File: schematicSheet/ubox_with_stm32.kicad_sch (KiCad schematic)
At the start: 14 parts, among them U3 SAM-M10Q-00B

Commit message: Arranged pin
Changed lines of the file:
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@@
 		(effects
 			(font
-				(size 1.27 1.27)
+				(size 0.889 0.889)
 			)
 			(justify left)
@@
 		(effects
 			(font
-				(size 1.27 1.27)
+				(size 0.889 0.889)
 			)
 			(justify left)
@@
 			(effects
 				(font
-					(size 1.27 1.27)
+					(size 0.889 0.889)
 				)
 				(justify left)
@@
 			(effects
 				(font
-					(size 1.27 1.27)
+					(size 0.889 0.889)
 				)
 				(justify left)
@@
 			(effects
 				(font
-					(size 1.27 1.27)
+					(size 0.889 0.889)
 				)
 			)
@@
 			(effects
 				(font
-					(size 1.27 1.27)
+					(size 0.889 0.889)
 				)
 				(justify left)
@@
 			(effects
 				(font
-					(size 1.27 1.27)
+					(size 0.889 0.889)
 				)
 				(justify left)
@@
 			(effects
 				(font
-					(size 1.27 1.27)
+					(size 0.889 0.889)
 				)
 			)
@@
 			(effects
 				(font
-					(size 1.27 1.27)
+					(size 0.889 0.889)
 				)
 			)
@@
 			(effects
 				(font
-					(size 1.27 1.27)
+					(size 0.889 0.889)
 				)
 			)
@@
 			(effects
 				(font
-					(size 1.27 1.27)
+					(size 0.889 0.889)
 				)
 			)
@@
 			(effects
 				(font
-					(size 1.27 1.27)
+					(size 0.889 0.889)
 				)
 				(justify right)
@@
 			(effects
 				(font
-					(size 1.27 1.27)
+					(size 0.889 0.889)
 				)
 				(justify right)
@@
 			(effects
 				(font
-					(size 1.27 1.27)
+					(size 0.889 0.889)
 				)
 				(justify right)
@@
 			(effects
 				(font
-					(size 1.27 1.27)
+					(size 0.889 0.889)
 				)
 				(justify right)
@@
 			(effects
 				(font
-					(size 1.27 1.27)
+					(size 0.889 0.889)
 				)
 			)
@@
 			(effects
 				(font
-					(size 1.27 1.27)
+					(size 0.889 0.889)
 				)
 			)
@@
 			(effects
 				(font
-					(size 1.27 1.27)
+					(size 0.889 0.889)
 				)
 			)
@@
 			(effects
 				(font
-					(size 1.27 1.27)
+					(size 0.889 0.889)
 				)
 			)
@@
 			(effects
 				(font
-					(size 1.27 1.27)
+					(size 0.889 0.889)
 				)
 				(justify left)
@@
 			(effects
 				(font
-					(size 1.27 1.27)
+					(size 0.889 0.889)
 				)
 				(justify left)
@@
 			(effects
 				(font
-					(size 1.27 1.27)
+					(size 0.889 0.889)
 				)
 			)
@@
 			(effects
 				(font
-					(size 1.27 1.27)
+					(size 0.889 0.889)
 				)
 			)
@@
 			(effects
 				(font
-					(size 1.27 1.27)
+					(size 0.889 0.889)
 				)
 				(justify left)
@@
 			(effects
 				(font
-					(size 1.27 1.27)
+					(size 0.889 0.889)
 				)
 				(justify left)
@@
 			(effects
 				(font
-					(size 1.27 1.27)
+					(size 0.889 0.889)
 				)
 			)
@@
 			(effects
 				(font
-					(size 1.27 1.27)
+					(size 0.889 0.889)
 				)
 			)
@@
 			(effects
 				(font
-					(size 1.524 1.524)
+					(size 0.889 0.889)
 				)
 			)
@@
 			(effects
 				(font
-					(size 1.524 1.524)
+					(size 0.889 0.889)
 				)
 			)
@@
 			(effects
 				(font
-					(size 1.27 1.27)
+					(size 0.889 0.889)
 				)
 				(justify right)
@@
 			(effects
 				(font
-					(size 1.27 1.27)
+					(size 0.889 0.889)
 				)
 				(justify right)
@@
 			(effects
 				(font
-					(size 1.27 1.27)
+					(size 0.889 0.889)
 				)
 			)
@@
 			(effects
 				(font
-					(size 1.27 1.27)
+					(size 0.889 0.889)
 				)
 			)
@@
 			(effects
 				(font
-					(size 1.27 1.27)
+					(size 0.889 0.889)
 				)
 			)
@@
 			(effects
 				(font
-					(size 1.27 1.27)
+					(size 0.889 0.889)
 				)
 			)
@@
 			(effects
 				(font
-					(size 1.27 1.27)
+					(size 0.889 0.889)
 				)
 			)
@@
 			(effects
 				(font
-					(size 1.27 1.27)
+					(size 0.889 0.889)
 				)
 				(justify left)
@@
 			(effects
 				(font
-					(size 1.27 1.27)
+					(size 0.889 0.889)
 				)
 				(justify left)

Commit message: update
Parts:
- C1, C2: footprint Capacitor_SMD:C_0805_2012Metric -> Capacitor_SMD:C_0402_1005Metric
- R1, R2, R3, R8, R9: footprint Resistor_SMD:R_0805_2012Metric -> Resistor_SMD:R_0402_1005Metric
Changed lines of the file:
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@@
 			)
 		)
-		(property "Footprint" "Resistor_SMD:R_0805_2012Metric"
+		(property "Footprint" "Resistor_SMD:R_0402_1005Metric"
 			(at 117.602 124.46 90)
 			(effects
@@
 			)
 		)
-		(property "Footprint" "Capacitor_SMD:C_0805_2012Metric"
+		(property "Footprint" "Capacitor_SMD:C_0402_1005Metric"
 			(at 100.0252 60.96 0)
 			(effects
@@
 			)
 		)
-		(property "Footprint" "Resistor_SMD:R_0805_2012Metric"
+		(property "Footprint" "Resistor_SMD:R_0402_1005Metric"
 			(at 203.2 59.182 90)
 			(effects
@@
 			)
 		)
-		(property "Footprint" "Capacitor_SMD:C_0805_2012Metric"
+		(property "Footprint" "Capacitor_SMD:C_0402_1005Metric"
 			(at 197.8152 144.78 0)
 			(effects
@@
 			)
 		)
-		(property "Footprint" "Resistor_SMD:R_0805_2012Metric"
+		(property "Footprint" "Resistor_SMD:R_0402_1005Metric"
 			(at 203.2 56.642 90)
 			(effects
@@
 			)
 		)
-		(property "Footprint" "Resistor_SMD:R_0805_2012Metric"
+		(property "Footprint" "Resistor_SMD:R_0402_1005Metric"
 			(at 143.002 124.46 90)
 			(effects
@@
 			)
 		)
-		(property "Footprint" "Resistor_SMD:R_0805_2012Metric"
+		(property "Footprint" "Resistor_SMD:R_0402_1005Metric"
 			(at 183.642 121.92 90)
 			(effects

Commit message: update
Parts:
- removed JP1: SolderJumper_2_Bridged, Jumper:SolderJumper-2_P1.3mm_Open_Pad1.0x1.5mm, symbol Jumper:SolderJumper_2_Bridged
- removed JP2: ~, Jumper:SolderJumper-2_P1.3mm_Open_Pad1.0x1.5mm, symbol Jumper:SolderJumper_2_Bridged
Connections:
- net 3.3V is gone; now on net +3.3V: C2.1, D1.2 (A), U3.17 (VCC), U3.2 (V_IO)
- net PPS: now also R2.1
- net +3.3V: now reaches R3.1
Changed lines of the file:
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@@
-	(wire
-		(pts
-			(xy 130.81 115.57) (xy 129.54 115.57)
-		)
-		(stroke
-			(width 0)
-			(type default)
-		)
-	)
 	(wire
 		(pts
@@
 	(wire
 		(pts
-			(xy 157.48 115.57) (xy 154.94 115.57)
-		)
-		(stroke
-			(width 0)
-			(type default)
-		)
-	)
-	(wire
-		(pts
 			(xy 196.85 129.54) (xy 196.85 137.16)
 		)
@@
 	(wire
 		(pts
-			(xy 121.92 115.57) (xy 119.38 115.57)
+			(xy 119.38 115.57) (xy 130.81 115.57)
 		)
 		(stroke
@@
 	(wire
 		(pts
-			(xy 147.32 115.57) (xy 144.78 115.57)
+			(xy 144.78 115.57) (xy 157.48 115.57)
 		)
 		(stroke
@@
 	)
 	(symbol
-		(lib_id "Jumper:SolderJumper_2_Bridged")
-		(at 151.13 115.57 0)
-		(unit 1)
-		(exclude_from_sim yes)
-		(in_bom no)
-		(on_board yes)
-		(dnp no)
-		(property "Reference" "JP2"
-			(at 151.13 112.522 0)
-			(effects
-				(font
-					(size 0.889 0.889)
-				)
-			)
-		)
-		(property "Value" "~"
-			(at 151.13 113.03 0)
-			(effects
-				(font
-					(size 1.27 1.27)
-				)
-			)
-		)
-		(property "Footprint" "Jumper:SolderJumper-2_P1.3mm_Open_Pad1.0x1.5mm"
-			(at 151.13 115.57 0)
-			(effects
-				(font
-					(size 1.27 1.27)
-				)
-				(hide yes)
-			)
-		)
-		(property "Datasheet" "~"
-			(at 151.13 115.57 0)
-			(effects
-				(font
-					(size 1.27 1.27)
-				)
-				(hide yes)
-			)
-		)
-		(property "Description" "Solder Jumper, 2-pole, closed/bridged"
-			(at 151.13 115.57 0)
-			(effects
-				(font
-					(size 1.27 1.27)
-				)
-				(hide yes)
-			)
-		)
-		(pin "2"
-		)
-		(pin "1"
-		)
-		(instances
-			(project "ubox_with_stm32"
-				(path "/6a7a65ce-5267-4485-8e7e-6a8fa9e8b937"
-					(reference "JP2")
-					(unit 1)
-				)
-			)
-			(project "ubox_with_stm32"
-				(path "/f49728bb-5f62-4190-bb7d-54bb4c159a74/b24004bc-4f43-480a-bb87-150062de6500"
-					(reference "JP3")
-					(unit 1)
-				)
-			)
-		)
-	)
-	(symbol
 		(lib_id "power:VCC")
 		(at 128.27 36.83 0)
@@
 			)
 		)
-		(property "Value" "3.3V"
+		(property "Value" "+3.3V"
 			(at 128.27 31.75 0)
 			(effects
@@
 			)
 		)
-		(property "Value" "3.3V"
+		(property "Value" "+3.3V"
 			(at 99.06 48.26 0)
 			(effects
@@
 			)
 		)
-		(property "Value" "3.3V"
+		(property "Value" "+3.3V"
 			(at 196.85 31.75 0)
 			(effects
@@
 			)
 		)
-		(property "Value" "3.3V"
+		(property "Value" "+3.3V"
 			(at 157.48 105.41 0)
 			(effects
@@
 	)
 	(symbol
-		(lib_id "Jumper:SolderJumper_2_Bridged")
-		(at 125.73 115.57 0)
-		(unit 1)
-		(exclude_from_sim yes)
-		(in_bom no)
-		(on_board yes)
-		(dnp no)
-		(property "Reference" "JP1"
-			(at 125.73 112.522 0)
-			(effects
-				(font
-					(size 0.889 0.889)
-				)
-			)
-		)
-		(property "Value" "SolderJumper_2_Bridged"
-			(at 125.73 111.76 0)
-			(effects
-				(font
-					(size 1.27 1.27)
-				)
-				(hide yes)
-			)
-		)
-		(property "Footprint" "Jumper:SolderJumper-2_P1.3mm_Open_Pad1.0x1.5mm"
-			(at 125.73 115.57 0)
-			(effects
-				(font
-					(size 1.27 1.27)
-				)
-				(hide yes)
-			)
-		)
-		(property "Datasheet" "~"
-			(at 125.73 115.57 0)
-			(effects
-				(font
-					(size 1.27 1.27)
-				)
-				(hide yes)
-			)
-		)
-		(property "Description" "Solder Jumper, 2-pole, closed/bridged"
-			(at 125.73 115.57 0)
-			(effects
-				(font
-					(size 1.27 1.27)
-				)
-				(hide yes)
-			)
-		)
-		(pin "2"
-		)
-		(pin "1"
-		)
-		(instances
-			(project ""
-				(path "/6a7a65ce-5267-4485-8e7e-6a8fa9e8b937"
-					(reference "JP1")
-					(unit 1)
-				)
-			)
-			(project ""
-				(path "/f49728bb-5f62-4190-bb7d-54bb4c159a74/b24004bc-4f43-480a-bb87-150062de6500"
-					(reference "JP2")
-					(unit 1)
-				)
-			)
-		)
-	)
-	(symbol
 		(lib_id "power:VCC")
 		(at 185.42 105.41 0)
@@
 			)
 		)
-		(property "Value" "3.3V"
+		(property "Value" "+3.3V"
 			(at 185.42 100.33 0)
 			(effects

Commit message: reroute
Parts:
- removed Rechargeable1: 3.1V Battery, Battery:BatteryHolder_Seiko_MS621F, symbol Device:Battery
- added BT1: 3098, Battery3V_holder:BAT_3098, symbol Battery3V_holder:3098
- D2, D3: footprint LED_SMD:LED_0805_2012Metric -> LED_SMD:LED_0402_1005Metric
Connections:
- net Backup: now also BT1.P1, BT1.P2
- net GND: now also BT1.N
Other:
- note added: "3V Rechargeable Battery"

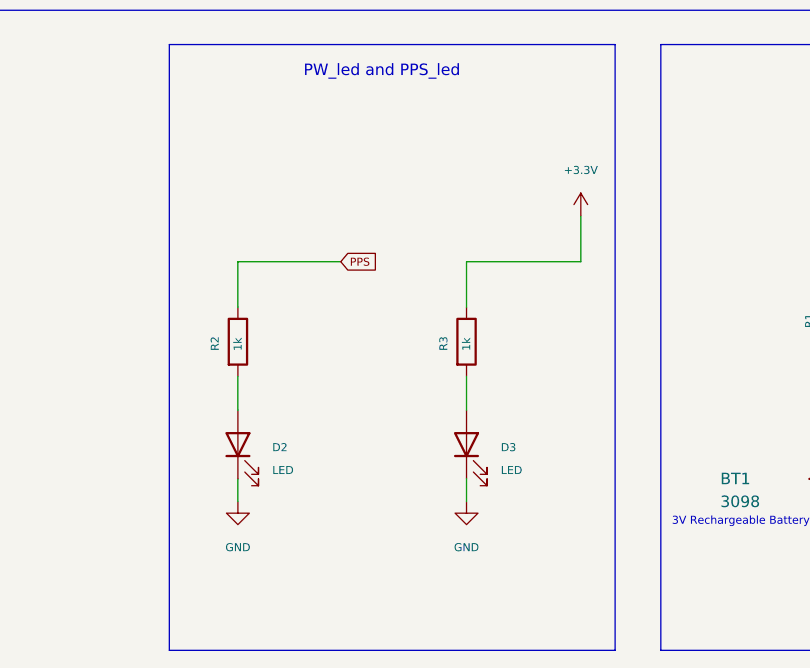
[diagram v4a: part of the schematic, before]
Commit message: rm led
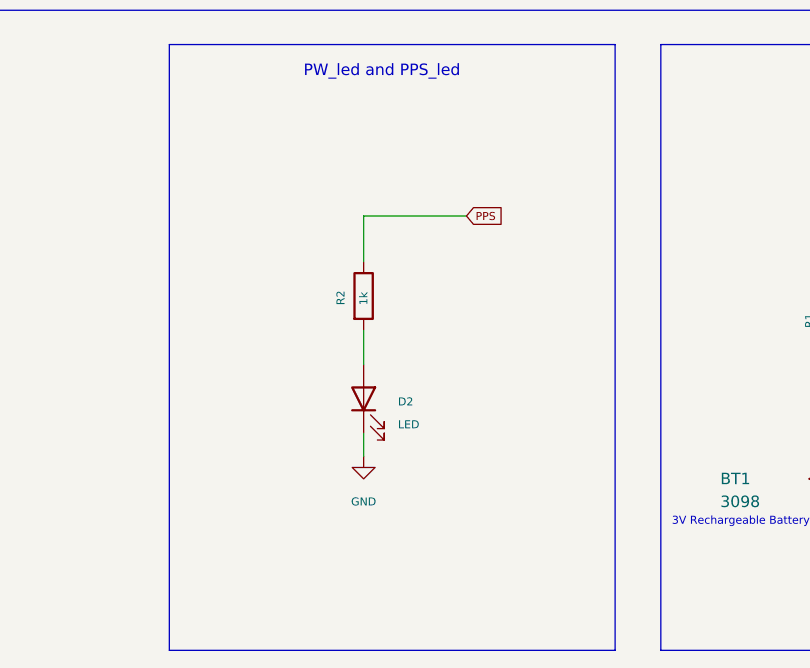
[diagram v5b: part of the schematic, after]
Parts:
- removed D3: LED, LED_SMD:LED_0402_1005Metric, symbol Device:LED
- removed R3: 1k, Resistor_SMD:R_0402_1005Metric, symbol Device:R
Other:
- moved on the sheet: D2, R2
